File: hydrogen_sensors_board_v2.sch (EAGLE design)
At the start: 44 parts, among them U1 ATMEGA328P_TQFP, U2 TLV1117-33IDCY, Y1 16MHz

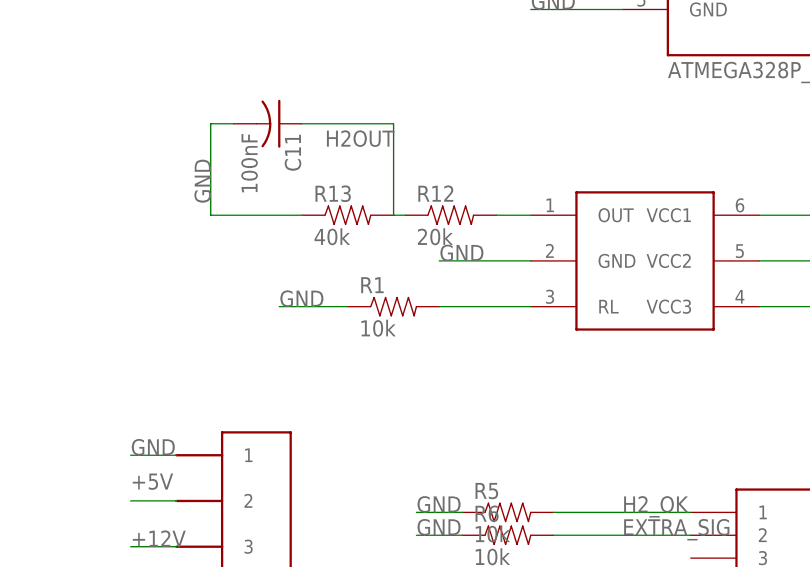
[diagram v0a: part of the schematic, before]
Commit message: changed a resistor value to a standard value
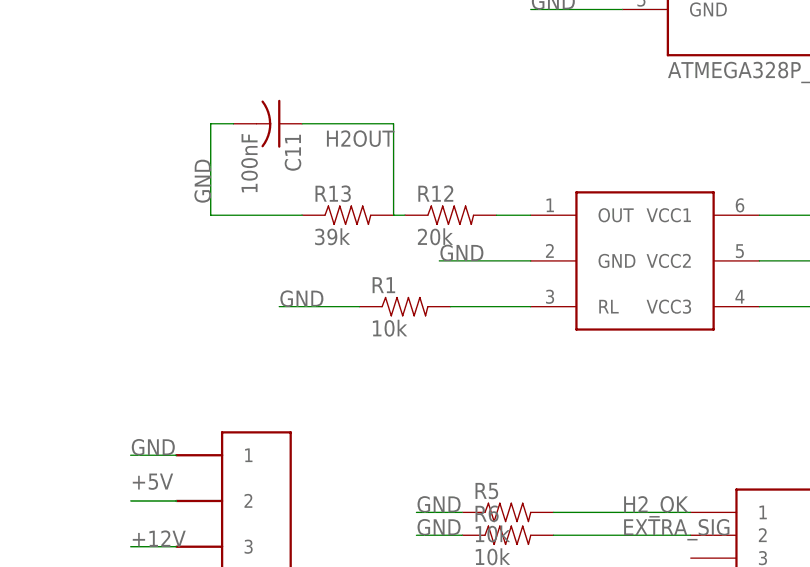
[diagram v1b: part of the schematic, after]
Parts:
- R13: value 40k -> 39k
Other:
- moved on the sheet: R1
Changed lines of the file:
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@@
 <?xml version="1.0" encoding="utf-8"?>
 <!DOCTYPE eagle SYSTEM "eagle.dtd">
-<eagle version="8.3.1">
+<eagle version="8.4.1">
 <drawing>
 <settings>
@@
 <part name="C10" library="adafruit" deviceset="C-US" device="C0603" value="10nF"/>
 <part name="R12" library="SparkFun-Passives" deviceset="RESISTOR" device="0603-RES" value="20k"/>
-<part name="R13" library="SparkFun-Passives" deviceset="RESISTOR" device="0603-RES" value="40k"/>
+<part name="R13" library="SparkFun-Passives" deviceset="RESISTOR" device="0603-RES" value="39k"/>
 <part name="C11" library="adafruit" deviceset="C-US" device="C0603" value="100nF"/>
 <part name="E1" library="5555140-6 RJ11" deviceset="5555140-6" device=""/>
@@
 <instance part="FRAME1" gate="G$2" x="172.72" y="0"/>
 <instance part="U1" gate="U$1" x="119.38" y="132.08"/>
-<instance part="R1" gate="G$1" x="68.58" y="73.66"/>
+<instance part="R1" gate="G$1" x="69.85" y="73.66"/>
 <instance part="ISP1" gate="G$1" x="177.8" y="78.74"/>
 <instance part="Y1" gate="G$1" x="88.9" y="134.62" rot="R90"/>
@@
 <segment>
 <pinref part="R1" gate="G$1" pin="1"/>
-<wire x1="63.5" y1="73.66" x2="55.88" y2="73.66" width="0.1524" layer="91"/>
+<wire x1="64.77" y1="73.66" x2="55.88" y2="73.66" width="0.1524" layer="91"/>
 <label x="55.88" y="73.66" size="1.778" layer="95"/>
 </segment>
@@
 <segment>
 <pinref part="U$1" gate="G$1" pin="RL"/>
-<wire x1="83.82" y1="73.66" x2="73.66" y2="73.66" width="0.1524" layer="91"/>
+<wire x1="83.82" y1="73.66" x2="74.93" y2="73.66" width="0.1524" layer="91"/>
 <pinref part="R1" gate="G$1" pin="2"/>
 </segment>
